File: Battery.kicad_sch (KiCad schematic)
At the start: 23 parts, among them J1 Battery, Q3 G230P06K, SW3 ON/OFF, U6 INA228, U7 AMS1117-3.3, U8 TPS82130

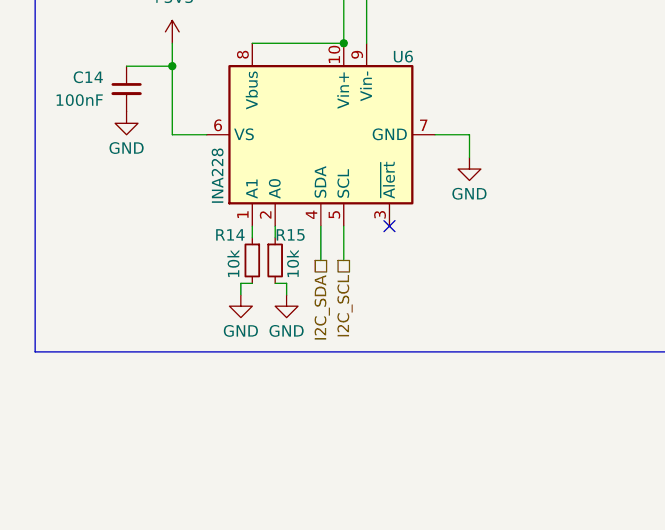
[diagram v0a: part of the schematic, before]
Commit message: Schematic updated for V2.0, updating PCB now
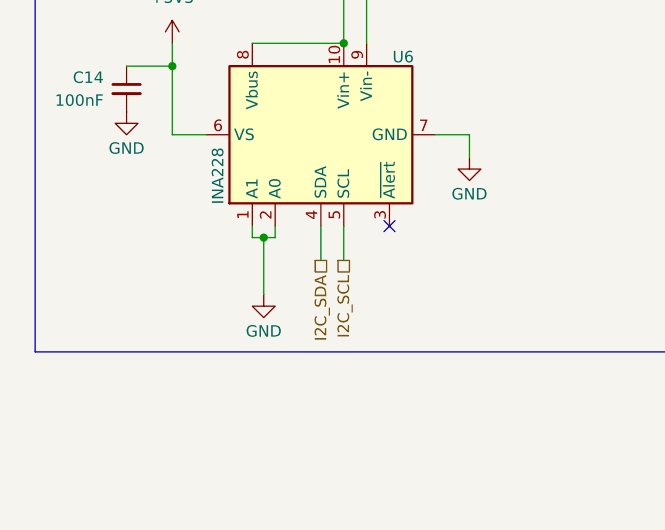
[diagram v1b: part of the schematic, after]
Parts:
- removed R14, R15: 10k, Resistor_SMD:R_0402_1005Metric, symbol Device:R_Small
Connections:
- net GND: now also U6.1 (A1), U6.2 (A0)
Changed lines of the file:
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@@
 		(title "Smart Key Cutter")
 		(date "2025-05-21")
-		(rev "1")
+		(rev "2")
 		(company "Ingenium Engineering Solutions")
 		(comment 1 "Purak Patel")
@@
 	)
 	(junction
+		(at 50.8 83.82)
+		(diameter 0)
+		(color 0 0 0 0)
+	)
+	(junction
 		(at 191.77 40.64)
 		(diameter 0)
@@
 	(wire
 		(pts
-			(xy 53.34 90.17) (xy 53.34 88.9)
-		)
-		(stroke
-			(width 0)
-			(type default)
-		)
-	)
-	(wire
-		(pts
 			(xy 49.53 82.55) (xy 49.53 83.82)
 		)
@@
 	(wire
 		(pts
-			(xy 48.26 90.17) (xy 48.26 88.9)
+			(xy 161.29 90.17) (xy 167.64 90.17)
 		)
 		(stroke
@@
 	(wire
 		(pts
-			(xy 161.29 90.17) (xy 167.64 90.17)
+			(xy 67.31 39.37) (xy 67.31 57.15)
 		)
 		(stroke
@@
 	(wire
 		(pts
-			(xy 67.31 39.37) (xy 67.31 57.15)
+			(xy 59.69 57.15) (xy 59.69 62.23)
 		)
 		(stroke
@@
 	(wire
 		(pts
-			(xy 59.69 57.15) (xy 59.69 62.23)
+			(xy 223.52 87.63) (xy 223.52 90.17)
 		)
 		(stroke
@@
 	(wire
 		(pts
-			(xy 223.52 87.63) (xy 223.52 90.17)
+			(xy 168.91 100.33) (xy 172.72 100.33)
 		)
 		(stroke
@@
 	(wire
 		(pts
-			(xy 168.91 100.33) (xy 172.72 100.33)
+			(xy 50.8 83.82) (xy 52.07 83.82)
 		)
 		(stroke
@@
 	(wire
 		(pts
+			(xy 50.8 83.82) (xy 49.53 83.82)
+		)
+		(stroke
+			(width 0)
+			(type default)
+		)
+	)
+	(wire
+		(pts
 			(xy 193.04 95.25) (xy 203.2 95.25)
 		)
@@
 	(wire
 		(pts
-			(xy 53.34 88.9) (xy 52.07 88.9)
+			(xy 50.8 90.17) (xy 50.8 83.82)
 		)
 		(stroke
@@
 	(wire
 		(pts
-			(xy 48.26 88.9) (xy 49.53 88.9)
-		)
-		(stroke
-			(width 0)
-			(type default)
-		)
-	)
-	(wire
-		(pts
 			(xy 109.22 39.37) (xy 113.03 39.37)
 		)
@@
 	(symbol
 		(lib_id "power:GND")
-		(at 48.26 90.17 0)
+		(at 50.8 90.17 0)
 		(unit 1)
 		(exclude_from_sim no)
@@
 		(dnp no)
 		(property "Reference" "#PWR031"
-			(at 48.26 96.52 0)
+			(at 50.8 96.52 0)
 			(effects
 				(font
@@
 		)
 		(property "Value" "GND"
-			(at 48.26 94.234 0)
+			(at 50.8 94.234 0)
 			(effects
 				(font
@@
 		)
 		(property "Footprint" ""
-			(at 48.26 90.17 0)
+			(at 50.8 90.17 0)
 			(effects
 				(font
@@
 		)
 		(property "Datasheet" ""
-			(at 48.26 90.17 0)
+			(at 50.8 90.17 0)
 			(effects
 				(font
@@
 		)
 		(property "Description" "Power symbol creates a global label with name \"GND\" , ground"
-			(at 48.26 90.17 0)
+			(at 50.8 90.17 0)
 			(effects
 				(font
@@
 	)
 	(symbol
-		(lib_id "Device:R_Small")
-		(at 49.53 86.36 0)
-		(mirror y)
-		(unit 1)
-		(exclude_from_sim no)
-		(in_bom yes)
-		(on_board yes)
-		(dnp no)
-		(property "Reference" "R14"
-			(at 48.768 83.566 0)
-			(effects
-				(font
-					(size 1.27 1.27)
-				)
-				(justify left)
-			)
-		)
-		(property "Value" "10k"
-			(at 47.498 88.392 90)
-			(effects
-				(font
-					(size 1.27 1.27)
-				)
-				(justify left)
-			)
-		)
-		(property "Footprint" "Resistor_SMD:R_0402_1005Metric"
-			(at 49.53 86.36 0)
-			(effects
-				(font
-					(size 1.27 1.27)
-				)
-				(hide yes)
-			)
-		)
-		(property "Datasheet" "~"
-			(at 49.53 86.36 0)
-			(effects
-				(font
-					(size 1.27 1.27)
-				)
-				(hide yes)
-			)
-		)
-		(property "Description" "Resistor, small symbol"
-			(at 49.53 86.36 0)
-			(effects
-				(font
-					(size 1.27 1.27)
-				)
-				(hide yes)
-			)
-		)
-		(pin "2"
-		)
-		(pin "1"
-		)
-		(instances
-			(project "Smart Key Cutter Interface"
-				(path "/e7f6820c-98d8-4aa2-b050-9c8bdbf7cc14/a0a04b63-6aa5-4f2b-9f02-0adccdc68a6b"
-					(reference "R14")
-					(unit 1)
-				)
-			)
-		)
-	)
-	(symbol
 		(lib_id "Regulator_Linear:AMS1117-3.3")
 		(at 175.26 40.64 0)
@@
 	)
 	(symbol
-		(lib_id "Device:R_Small")
-		(at 52.07 86.36 0)
-		(unit 1)
-		(exclude_from_sim no)
-		(in_bom yes)
-		(on_board yes)
-		(dnp no)
-		(property "Reference" "R15"
-			(at 52.07 83.566 0)
-			(effects
-				(font
-					(size 1.27 1.27)
-				)
-				(justify left)
-			)
-		)
-		(property "Value" "10k"
-			(at 54.102 88.392 90)
-			(effects
-				(font
-					(size 1.27 1.27)
-				)
-				(justify left)
-			)
-		)
-		(property "Footprint" "Resistor_SMD:R_0402_1005Metric"
-			(at 52.07 86.36 0)
-			(effects
-				(font
-					(size 1.27 1.27)
-				)
-				(hide yes)
-			)
-		)
-		(property "Datasheet" "~"
-			(at 52.07 86.36 0)
-			(effects
-				(font
-					(size 1.27 1.27)
-				)
-				(hide yes)
-			)
-		)
-		(property "Description" "Resistor, small symbol"
-			(at 52.07 86.36 0)
-			(effects
-				(font
-					(size 1.27 1.27)
-				)
-				(hide yes)
-			)
-		)
-		(pin "2"
-		)
-		(pin "1"
-		)
-		(instances
-			(project "Smart Key Cutter Interface"
-				(path "/e7f6820c-98d8-4aa2-b050-9c8bdbf7cc14/a0a04b63-6aa5-4f2b-9f02-0adccdc68a6b"
-					(reference "R15")
-					(unit 1)
-				)
-			)
-		)
-	)
-	(symbol
 		(lib_id "power:GND")
 		(at 104.14 57.15 0)
@@
 					(unit 1)
 				)
-			)
-		)
-	)
-	(symbol
-		(lib_id "power:GND")
-		(at 53.34 90.17 0)
-		(unit 1)
-		(exclude_from_sim no)
-		(in_bom yes)
-		(on_board yes)
-		(dnp no)
-		(property "Reference" "#PWR033"
-			(at 53.34 96.52 0)
-			(effects
-				(font
-					(size 1.27 1.27)
-				)
-				(hide yes)
-			)
-		)
-		(property "Value" "GND"
-			(at 53.34 94.234 0)
-			(effects
-				(font
-					(size 1.27 1.27)
-				)
-			)
-		)
-		(property "Footprint" ""
-			(at 53.34 90.17 0)
-			(effects
-				(font
-					(size 1.27 1.27)
-				)
-				(hide yes)
-			)
-		)
-		(property "Datasheet" ""
-			(at 53.34 90.17 0)
-			(effects
-				(font
-					(size 1.27 1.27)
-				)
-				(hide yes)
-			)
-		)
-		(property "Description" "Power symbol creates a global label with name \"GND\" , ground"
-			(at 53.34 90.17 0)
-			(effects
-				(font
-					(size 1.27 1.27)
-				)
-				(hide yes)
-			)
-		)
-		(pin "1"
-		)
-		(instances
-			(project "Smart Key Cutter Interface"
-				(path "/e7f6820c-98d8-4aa2-b050-9c8bdbf7cc14/a0a04b63-6aa5-4f2b-9f02-0adccdc68a6b"
-					(reference "#PWR033")
-					(unit 1)
-				)

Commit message: Version 2 sent to JLC
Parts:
- added TP1: TestPoint, Ingenium:RH-5015, symbol Connector:TestPoint
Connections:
- net +3V3: now also TP1.1
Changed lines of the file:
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@@
+	)
+	(symbol
+		(lib_id "Connector:TestPoint")
+		(at 191.77 40.64 0)
+		(unit 1)
+		(exclude_from_sim no)
+		(in_bom yes)
+		(on_board yes)
+		(dnp no)
+		(property "Reference" "TP1"
+			(at 190.246 35.306 0)
+			(effects
+				(font
+					(size 1.27 1.27)
+				)
+				(justify left)
+			)
+		)
+		(property "Value" "TestPoint"
+			(at 187.198 34.544 0)
+			(effects
+				(font
+					(size 1.27 1.27)
+				)
+				(justify left)
+				(hide yes)
+			)
+		)
+		(property "Footprint" "Ingenium:RH-5015"
+			(at 196.85 40.64 0)
+			(effects
+				(font
+					(size 1.27 1.27)
+				)
+				(hide yes)
+			)
+		)
+		(property "Datasheet" "~"
+			(at 196.85 40.64 0)
+			(effects
+				(font
+					(size 1.27 1.27)
+				)
+				(hide yes)
+			)
+		)
+		(property "Description" "test point"
+			(at 191.77 40.64 0)
+			(effects
+				(font
+					(size 1.27 1.27)
+				)
+				(hide yes)
+			)
+		)
+		(pin "1"
+		)
+		(instances
+			(project ""
+				(path "/e7f6820c-98d8-4aa2-b050-9c8bdbf7cc14/a0a04b63-6aa5-4f2b-9f02-0adccdc68a6b"
+					(reference "TP1")
+					(unit 1)
+				)
+			)
+		)
 	)
 	(symbol
